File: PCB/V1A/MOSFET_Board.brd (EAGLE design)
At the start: 230 x 115 mm, 276 parts, among them IC301 7805T, IC302 7805T, J301 +12V, J302 FAN_MOLEX4PIN, J303 FAN_MOLEX4PIN, J304 DUT+, J305 DUT-, Q201 SIRC10DP, Q202 SIRC10DP, Q203 BC817, Q204 BC817, Q205 SIRC10DP, Q206 SIRC10DP, Q207 BC817, Q208 BC807, Q209 BC817, Q210 BC807, Q211 IXTK102N65X2, Q212 IXTK102N65X2, Q301 BC817, Q302 BC817, Q401 BC807, Q402 BC807, Q403 BC807, Q404 BC807, Q405 BC807, Q406 BC807, Q407 BC807, Q408 BC807, Q409 BC807, Q410 BC807, Q411 BC807, Q412 BC807, Q413 BC807, Q414 BC807, U201 AD420, U202 AD420, U203 LT1014I, U204 LT1014I, U205 AD620, U206 AD620, U207 AD620, U208 AD620, U209 LTC1865L, U210 LTC1865L, U301 LP2985-3.1, U302 LP2985-3.1, U303 AD620, U304 LTC1865L, U305 LTC1865L, U306 MAX743, U401 HCPL-063N, U402 HCPL-063N, U403 HCPL-063N, U404 HCPL-063N, U405 HCPL-063N, U406 HCPL-063N, U407 HCPL-063N

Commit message: PCB layout
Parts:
- removed HS201, HS202: (no value), mechanical:HEATSINK-LGA115X
- added C1, C2: 4µ7, passives:C3216
- added C3: 10n, passives:C2012
- added HS1: HEATSINK_LGA775, mechanical:D95263-001
- added HS2: HEATSINK_LGA115X, mechanical:E97378-001
- added U1: LP2985-3.1, ic:SOT23-5L
- JP301: device pinhead:2X03 -> mechanical:HEAD_MALE_2X3
- JP302: device pinhead:1X16 -> mechanical:HEAD_MALE_1X16
- moved R235 19.7 mm to (44.0, 2.00), turned to 270 degrees
- moved R231 19.4 mm to (44.0, 7.00), turned to 90 degrees
- moved R237 16.3 mm to (46.5, 2.00), turned to 270 degrees
- moved Q203 13.5 mm to (48.0, 7.00), turned to 180 degrees
- moved C215 13.1 mm to (49.0, 2.00), turned to 90 degrees
- moved C210 9.75 mm to (29.0, -5.75), flipped to the top, turned to 180 degrees
- moved C214 9.62 mm to (29.0, -3.50), flipped to the top, turned to 180 degrees
- moved Q207 8.50 mm to (53.0, 2.00), turned to 180 degrees
- moved D203 6.92 mm to (85.0, 2.00), turned to 180 degrees
- moved D204 6.91 mm to (61.5, 2.00), turned to 180 degrees
- moved Q208 6.40 mm to (53.0, 7.00), turned to 180 degrees
- moved C212 5.00 mm to (29.0, -8.00), flipped to the top, turned to 180 degrees
- moved C302 5.00 mm to (40.0, -4.00)
- moved C305 5.00 mm to (44.0, -1.00)
- moved C307 5.00 mm to (48.0, -4.00)
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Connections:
- new net N$66: C3.1, U1.4
- net +3V3: now also C2.1, U1.5
- net +5V: now also C1.1, U1.1, U1.3
- net GND: now also C1.2, C2.2, C3.2, U1.2
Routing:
- net +5V: track 178.9 -> 340.6 mm, vias 34 -> 36
- net CONV_C2: track 14.7 -> 134.8 mm, vias 0 -> 2
- net BYP: track 14.7 -> 131.5 mm, vias 0 -> 2
- net +12V: track 102.1 -> 202.4 mm, vias 1 -> 3
- net +3V3: track 9.05 -> 103.6 mm, vias 6 -> 7
- net CONV_V: track 53.9 -> 148.2 mm
- net CLR_DAC2: track 16.5 -> 102.5 mm, vias 1 -> 2
- net +3V_2: track 21.6 -> 80.7 mm, vias 3 -> 7
- net CONV_TEMP: track 14.7 -> 69.8 mm, vias 0 -> 2
- net GND: track 253.3 -> 308.3 mm, vias 90 -> 103
- net DUT-: track 28.3 -> 78.4 mm
- net CONV_C1: track 14.7 -> 47.9 mm, vias 0 -> 2
- net VREF2: track 10.1 -> 42.4 mm
- net -15V: track 43.0 -> 72.1 mm
- net +15V: track 89.5 -> 115.9 mm
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- removed copper zone on layer 16, net BYP2

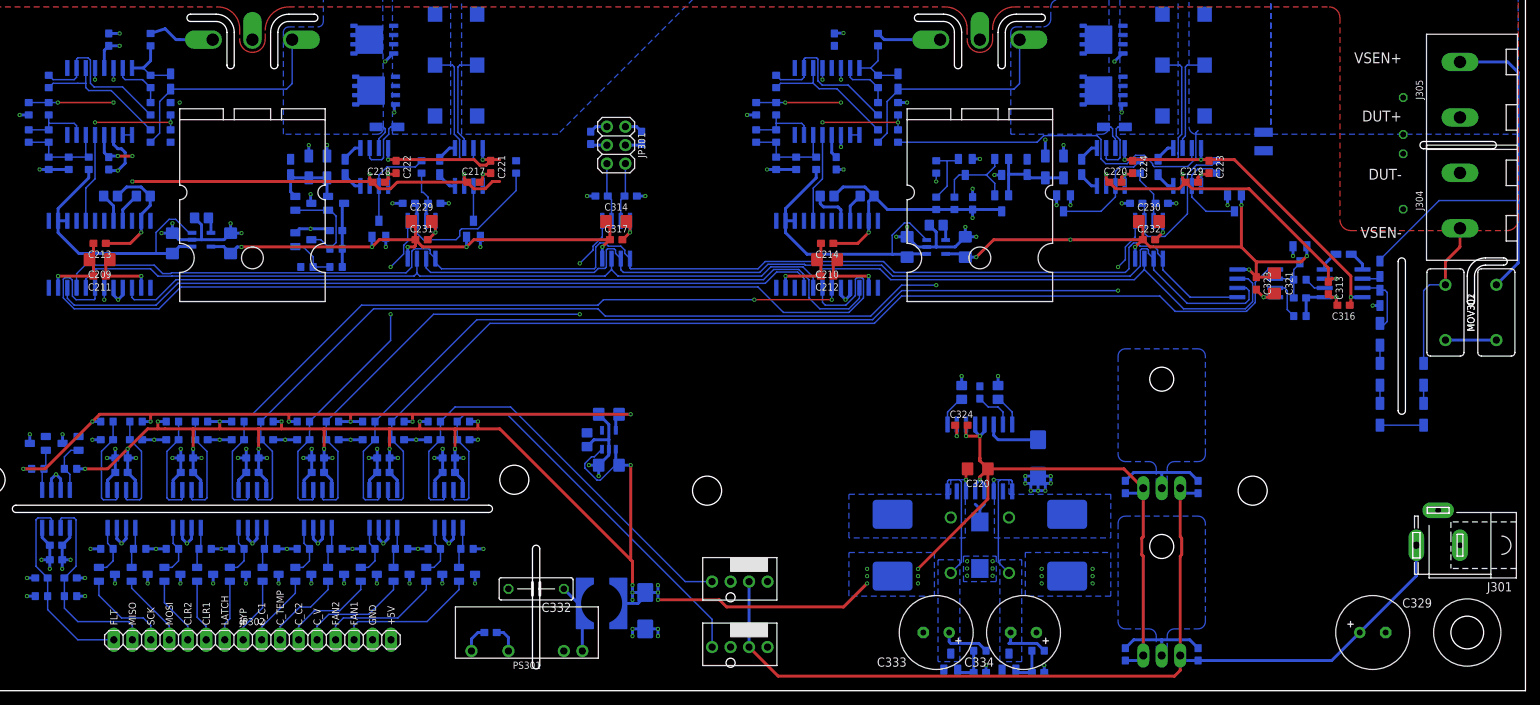
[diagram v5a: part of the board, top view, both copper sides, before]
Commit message: Finished first pass routing/layout
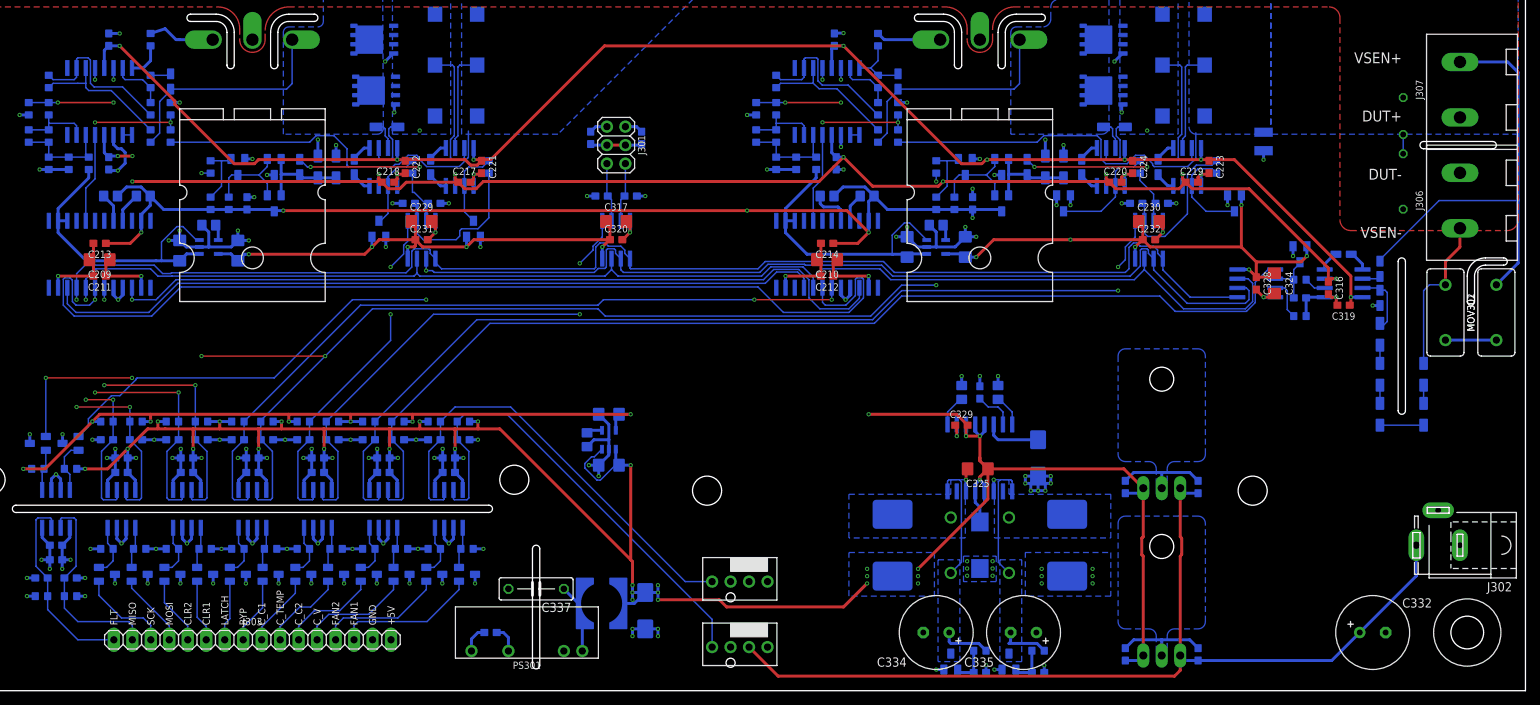
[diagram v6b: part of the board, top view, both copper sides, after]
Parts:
- removed C1, C2: 4µ7, passives:C3216
- removed C3: 10n, passives:C2012
- removed JP301: TEMP, mechanical:HEAD_MALE_2X3
- removed JP302: CTRL, mechanical:HEAD_MALE_1X16
- removed U1: LP2985-3.1, ic:SOT23-5L
- added C338, C339: 470n, passives:C1608
- added C340: 100n, passives:C1608
- added J306: DUT+, mechanical:AMPHENOL-12-762_2
- added J307: DUT-, mechanical:AMPHENOL-12-762_2
- added U307: MAX743, ic:SO16W
- C303, C317, C324: value 100n -> 4µ7; device passives:C1608 -> passives:C3216
- C304, C328: value 10n -> 100n; device passives:C2012 -> passives:C1608
- C306, C307: value 4µ7 -> 10n; device passives:C3216 -> passives:C2012
- C308, C309, C310, C325: value 470n -> 4µ7; device passives:C1608 -> passives:C3216
- C311, C313: value 100n -> 470n
- C314, C320, C321: value 4µ7 -> 100n; device passives:C3216 -> passives:C1608
- C315: value 470p -> 470n
- C318: value 100n -> 470p
- C322: value 47µ -> 100n; device passives:CT7343 -> passives:C1608
- C323: value 100n -> 47µ; device passives:C1608 -> passives:CT7343
- C329: value 220µ -> 100n; device rcl:E3,5-10 -> passives:C1608
- C330: value 10µ -> 470n; device passives:CT6032 -> passives:C1608
- C331: value 150n -> 10n; device rcl:C050-030X075 -> passives:C2012
- C332: value 470p -> 220µ; device rcl:C075-032X103 -> rcl:E3,5-10
- C333: value 220µ -> 10µ; device rcl:E3,5-10 -> passives:CT6032
- C335: value 100n -> 220µ; device passives:C1608 -> rcl:E3,5-10
- C336: value 470n -> 150n; device passives:C1608 -> rcl:C050-030X075
- C337: value 470n -> 470p; device passives:C1608 -> rcl:C075-032X103
- J301: value +12V -> TEMP; device con-jack:SPC4078 -> mechanical:HEAD_MALE_2X3
- J302: value FAN_MOLEX4PIN -> +12V; device mechanical:MOLEX_47053-1000 -> con-jack:SPC4078
- J303: value FAN_MOLEX4PIN -> CTRL; device mechanical:MOLEX_47053-1000 -> mechanical:HEAD_MALE_1X16
- J304: value DUT+ -> FAN_MOLEX4PIN; device mechanical:AMPHENOL-12-762_2 -> mechanical:MOLEX_47053-1000
- J305: value DUT- -> FAN_MOLEX4PIN; device mechanical:AMPHENOL-12-762_2 -> mechanical:MOLEX_47053-1000
- L302: value 4µ7 -> 100µ; device inductor-coilcraft:MSS7341 -> passives:MSS1260
- L303: value 100µ -> 4µ7; device passives:MSS1260 -> inductor-coilcraft:MSS7341
- U303: value AD620 -> LP2985-3.1; device ic:SO8 -> ic:SOT23-5L
- U304: value LTC1865L -> AD620
- U306: value MAX743 -> LTC1865L; device ic:SO16W -> ic:SO8
- moved J301 125.7 mm to (0.00, 10.0), turned to 270 degrees
- moved J305 119.9 mm to (17.0, -50.0), turned to 0 degrees
- moved J304 116.5 mm to (17.0, -59.0), turned to 0 degrees
- moved C332 115.2 mm to (104.0, -57.0), turned to 0 degrees
- moved U303 103.3 mm to (-1.00, -30.5), turned to 0 degrees
- moved C312 100.3 mm to (80.0, -60.0), turned to 90 degrees
- moved U304 100.2 mm to (100.0, -9.00), turned to 270 degrees
- moved C305 100.0 mm to (-56.0, -1.00)
- moved C306 97.0 mm to (44.0, -1.00), turned to 0 degrees
- moved J302 97.0 mm to (113.0, -45.0), turned to 180 degrees
- moved C336 96.1 mm to (108.2, 14.0), turned to 90 degrees
- moved C315 93.1 mm to (2.00, 3.00)
- moved U305 88.2 mm to (0.00, -3.00), turned to 180 degrees
- moved C310 81.6 mm to (-1.00, -27.0), turned to 0 degrees
- moved C335 73.3 mm to (56.0, -57.0), flipped to the top
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- renumbered HS1 to HS201, HS2 to HS202
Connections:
- net +12V: now also C312.1, C313.1, C332.+, J302.3, J304.2, J305.2; no longer C309.1, C310.1, C329.+, J301.3, J302.2, J303.2
- net +15V: now also C316.1, Q302.2, U304.7; no longer C313.1, Q301.2, U303.7
- net +3V3: now also C310.1, U303.5; no longer C2.1, U1.5
- net +3V_1: now also C308.1, C320.1, U305.8; no longer C306.1, C314.1, U304.8
- net +3V_2: now also C309.1, C324.1, C328.1, U306.8; no longer C307.1, C321.1, C323.1, U305.8
- net +5V: now also C304.1, C314.1, C321.1, C322.1, C323.+, C325.1, C329.2, C333.+, J301.3, J301.4, L301.1, L303.2, U303.1, U303.3, U307.12, U307.13, U307.3, U307.4, U307.5; no longer C1.1, C311.1, C318.1, C319.1, C320.1, C322.+, C324.2, C330.+, JP301.3, JP301.4, L302.2, L303.1, U1.1, U1.3, U306.12, U306.13, U306.3, U306.4, U306.5
- net +5V_I: now also C337.2, C340.1, J303.16; no longer C332.2, C335.1, JP302.16
- net -15V: now also C319.1, Q301.2, U304.4; no longer C316.1, Q302.2, U303.4
- net BYP_I: now also J303.8; no longer JP302.8
- net CLR_DAC1_I: now also J303.6; no longer JP302.6
- net CLR_DAC2: now also C413.1, R413.1, U401.6; no longer C427.1, R427.1, U406.6
- net CLR_DAC2_I: now also J303.7, Q405.1; no longer JP302.5, Q413.1
- net CONV_C1_I: now also J303.9; no longer JP302.9
- net CONV_C2_I: now also J303.11; no longer JP302.11
- net CONV_TEMP: now also U305.1; no longer U304.1
- net CONV_TEMP_I: now also J303.10; no longer JP302.10
- net CONV_V: now also U306.1; no longer U305.1
- net CONV_V_I: now also J303.12; no longer JP302.12
- net DUT+: now also J306.2; no longer J304.2
- net DUT-: now also C336.2, J307.1; no longer C331.2, J305.1
- net FAN1_PWM: now also J304.4; no longer J302.4
- net FAN1_PWM_I: now also J303.14; no longer JP302.14
- net FAN1_SIG: now also J304.3; no longer J302.3
- net FAN2_PWM: now also J305.4; no longer J303.4
- net FAN2_PWM_I: now also J303.13; no longer JP302.13
- net FAN2_SIG: now also J305.3; no longer J303.3
- net FLT_DAC_I: now also J303.1; no longer JP302.1
- net GND: now also C322.2, C323.-, C324.2, C329.1, C330.2, C331.2, C332.-, C334.-, C335.+, C338.2, C339.2, J301.2, J304.1, J305.1, L302.2, U303.2, U304.5, U306.4, U307.11, U307.14, U307.2; no longer C1.2, C2.2, C3.2, C322.-, C323.2, C324.1, C329.-, C330.-, C334.+, C336.2, C337.2, J303.1, JP301.1, JP301.2, L301.2, U1.2, U303.5, U304.4, U306.11, U306.14, U306.2
- net GNDI: now also C340.2, J303.15; no longer C335.2, JP302.15
- net LATCH_DAC: now also C427.1, R427.1, U406.6; no longer C413.1, R413.1, U401.6
- net LATCH_DAC_I: now also J303.5, Q413.1; no longer JP302.7, Q405.1
- net MISO: now also U306.6; no longer U304.6
- net MISO_I: now also J303.2; no longer JP302.2
- net MOSI: now also U306.5; no longer U304.5
- net MOSI_I: now also J303.4; no longer JP302.4
- net N$10: now also C305.1; no longer C304.1
- net N$23: now also U304.6; no longer U303.6
- net N$29: now also U304.3; no longer U303.3
- net N$30: now also C318.1, U306.2; no longer C315.1, U305.2
- net N$32: now also C334.+, Q302.3, U307.16; no longer C333.+, Q301.3, U306.16
- net N$34: now also C331.1, U307.8; no longer C328.1, U306.8
- net N$35: now also C330.1, U307.7; no longer C325.1, U306.7
- net N$36: now also U304.2; no longer U303.2
- net N$37: now also U307.1; no longer U306.1
- net N$38: now also L301.2, U307.15; no longer L303.2, U306.15
- net N$39: now also L302.1, U307.10; no longer L301.1, U306.10
- net N$45: now also U306.3; no longer U305.3
- net N$60: now also C337.1, L303.1; no longer C332.1, L302.1
- net N$61: now also C336.1; no longer C331.1
- net N$62: now also C306.1; no longer C305.1
- net N$63: now also C339.1, Q302.1; no longer C336.1, Q301.1
- net N$64: now also C335.-, Q301.3, U307.9; no longer C334.-, Q302.3, U306.9
- net N$65: now also C338.1, Q301.1; no longer C337.1, Q302.1
- net N$66: now also C307.1, U303.4; no longer C3.1, U1.4
- net RG1_H6: now also U304.1; no longer U303.1
- net RG2_H6: now also U304.8; no longer U303.8
- net SCK: now also U306.7; no longer U304.7
- net SCK_I: now also J303.3; no longer JP302.3
- net TEMP1: now also C311.1, J301.5, U305.2; no longer C308.1, JP301.5, U304.2
- net TEMP2: now also C315.1, J301.6, U305.3; no longer C312.1, JP301.6, U304.3
- net VREF_MAX743: now also U307.6; no longer U306.6
- net VSENSE+: now also J306.1; no longer J304.1
- net VSENSE-: now also J307.2; no longer J305.2
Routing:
- net -15V: track 72.1 -> 292.1 mm, vias 6 -> 9
- net +15V: track 115.9 -> 274.3 mm, vias 8 -> 11
- net +12V: track 202.4 -> 345.5 mm, vias 3 -> 5
- net +5V: track 340.6 -> 447.8 mm, vias 36 -> 37
- net MISO: track 131.3 -> 191.8 mm, vias 0 -> 2
- net DUT-: track 78.4 -> 127.8 mm
- net BYP: track 131.5 -> 175.0 mm, vias 2 -> 5
- net LATCH_DAC: track 153.3 -> 184.0 mm, vias 0 -> 3
- net FLT_DAC: track 109.5 -> 139.8 mm, vias 0 -> 3
- net CLR_DAC1: track 16.3 -> 45.6 mm, vias 1 -> 3
- net MOSI: track 196.0 -> 221.6 mm, vias 0 -> 3
- net SCK: track 195.1 -> 217.3 mm, vias 0 -> 3
- net CSEN_H2: track 28.3 -> 50.0 mm, vias 0 -> 3
- net CSEN_H1: track 28.8 -> 49.9 mm, vias 0 -> 3
- net N$7: track 4.80 -> 11.3 mm
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
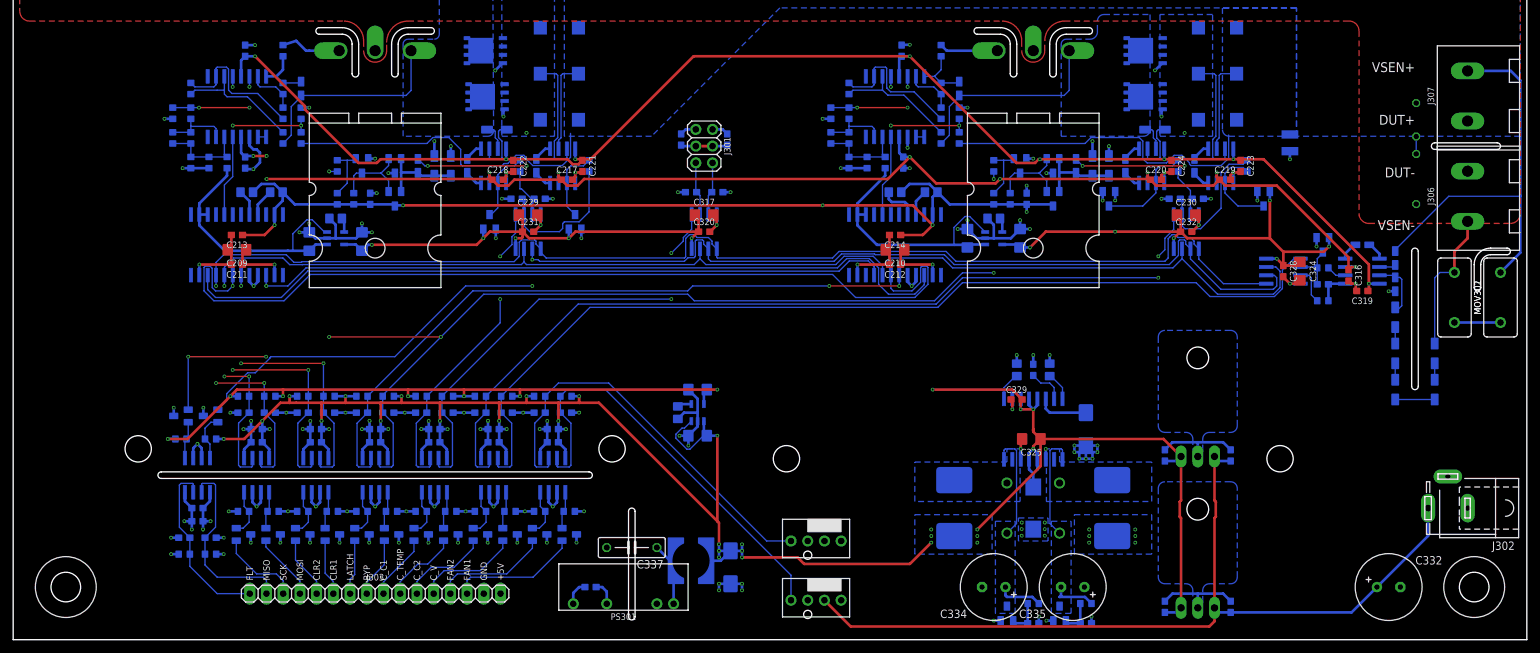
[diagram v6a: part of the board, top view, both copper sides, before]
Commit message: PCB layout
Added some copper pours.
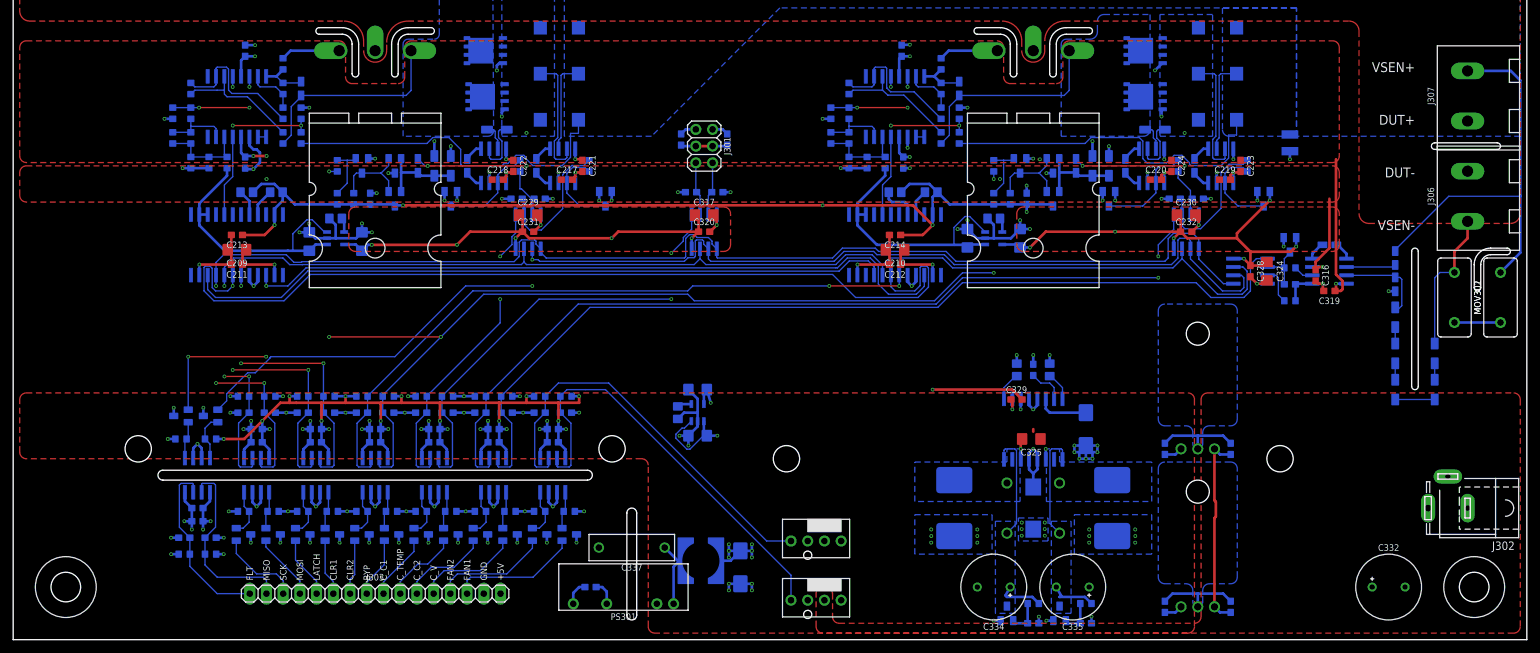
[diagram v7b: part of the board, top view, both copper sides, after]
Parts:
- removed C336: 150n, rcl:C050-030X075
- removed R311: 16R, rcl:0204/7
- C201, C202, C203, C204, C211, C212, C213, C214, C215, C216, C217, C218, C219, C220, C221, C222, C223, C224, C225, C226, C227, C228, C231, C232, C304, C311, C312, C313, C314, C315, C316, C318, C319, C320, C321, C322, C328, C329, C330, C338, C339, C340, C401, C402, C403, C404, C405, C406, C407, C408, C409, C410, C411, C412, C413, C414, C415, C416, C417, C418, C419, C420, C421, C422, C423, C424, C425, C426, C427, C428: device passives:C1608 -> passives:CAPC1608
- C205, C206, C207, C208, C305, C306, C307, C326, C331: device passives:C2012 -> passives:CAPC2012
- C209, C210, C229, C230, C301, C302, C303, C308, C309, C310, C317, C324, C325: device passives:C3216 -> passives:CAPC3216
- C323: device passives:CT7343 -> passives:CAPCP7343
- C327, C333: device passives:CT6032 -> passives:CAPCP6032
- C332, C334, C335: device rcl:E3,5-10 -> passives:CAPPRD500W60D1000H
- C337: device rcl:C075-032X103 -> passives:CAPRR1000W80L1300T400H900
- IC301, IC302: value 7805T -> 78L05_TO-220AB-3-BR; device linear:TO220H -> ic:TO-220AB-3-BR
- R201, R202, R203, R204, R205, R206, R207, R208, R209, R210, R211, R212, R213, R214, R215, R216, R217, R218, R219, R220, R221, R222, R223, R224, R225, R226, R229, R230, R231, R233, R235, R236, R237, R239, R255, R256, R257, R258, R309, R310, R312, R313, R401, R402, R403, R404, R405, R406, R407, R408, R409, R410, R411, R412, R413, R414, R415, R416, R417, R418, R419, R420, R421, R422, R423, R424, R425, R426, R427, R428: device passives:R1608 -> passives:RESC1608
- R227, R228, R247, R248, R251, R252, R253, R254, R302, R307, R308: device passives:R2012W -> passives:RESC2012
- R232, R234, R238, R240, R243, R245, R301, R303, R304, R305, R306: device passives:R3216W -> passives:RESC3216
- R241, R242, R244, R246, R249, R250: device passives:R6332W -> passives:RESC6332
- moved IC301 10.0 mm to (75.0, -60.0)
- moved IC302 9.00 mm to (75.0, -36.0)
- moved D202 6.85 mm to (-38.5, 2.00), turned to 180 degrees
- moved D201 5.79 mm to (-15.0, 2.00), turned to 180 degrees
- moved C316 5.00 mm to (92.9, -9.63)
- moved C318 5.00 mm to (89.0, -11.0)
- moved C319 5.00 mm to (95.0, -12.0)
- moved C324 5.00 mm to (85.5, -9.00)
- moved C328 5.00 mm to (83.0, -9.00)
- moved D301 5.00 mm to (89.0, -5.00)
- moved R308 5.00 mm to (95.0, -5.00)
- moved R309 5.00 mm to (89.0, -8.50)
- moved R310 5.00 mm to (89.0, -13.5)
- moved U304 5.00 mm to (95.0, -9.00)
- moved U306 5.00 mm to (83.0, -9.00)
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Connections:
- removed net N$61: C336.1, R311.1
- net DUT+: no longer R311.2
- net DUT-: no longer C336.2
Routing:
- net -15V: track 292.1 -> 115.7 mm
- net +15V: track 274.3 -> 104.2 mm
- net +5V: track 447.8 -> 298.7 mm
- net +12V: track 345.5 -> 244.3 mm
- net +3V3: track 103.6 -> 13.5 mm
- net +3V_1: track 71.2 -> 83.1 mm, vias 5 -> 7
- net DUT-: track 127.8 -> 134.6 mm
- net N$36: track 2.53 -> 7.53 mm
- net N$29: track 9.27 -> 14.3 mm
- net SCK: track 217.3 -> 212.6 mm
- net CONV_V: track 148.2 -> 144.0 mm
- net MOSI: track 221.6 -> 217.7 mm
- net N$16: track 11.2 -> 15.0 mm
- net MISO: track 191.8 -> 188.5 mm
- net +3V_2: track 80.7 -> 77.7 mm
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- added copper zone on layer 1, net +12V
- added copper zone on layer 1, net +15V
- added copper zone on layer 2, net +3V3
- added copper zone on layer 1, net +3V_1
- added copper zone on layer 1, net +3V_2
- added copper zone on layer 1, net +5V
- added copper zone on layer 1, net -15V
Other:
- outline, holes or cut-outs redrawn

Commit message: PCB layout
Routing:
- net -15V: track 115.7 -> 114.4 mm
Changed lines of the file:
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@@
 <layer number="13" name="Route13" color="21" fill="1" visible="no" active="no"/>
 <layer number="14" name="Route14" color="22" fill="1" visible="no" active="no"/>
-<layer number="15" name="Route15" color="23" fill="1" visible="no" active="yes"/>
+<layer number="15" name="Route15" color="23" fill="1" visible="yes" active="yes"/>
 <layer number="16" name="Bottom" color="1" fill="1" visible="yes" active="yes"/>
 <layer number="17" name="Pads" color="2" fill="1" visible="yes" active="yes"/>
@@
 <via x="-19.595" y="8" extent="1-16" drill="0.3" diameter="0.6"/>
 <wire x1="80.405" y1="9.6" x2="80.405" y2="8" width="0.4064" layer="16"/>
-<wire x1="81.5" y1="7.85" x2="81.35" y2="8" width="0.4064" layer="1"/>
 <via x="69.905" y="8" extent="1-16" drill="0.3" diameter="0.6"/>
-<wire x1="70" y1="8" x2="69.905" y2="8" width="0.4064" layer="1"/>
-<wire x1="70.85" y1="8" x2="71" y2="7.85" width="0.4064" layer="1"/>
 <wire x1="69.905" y1="9.6" x2="69.905" y2="8" width="0.4064" layer="16"/>
-<wire x1="71" y1="7.85" x2="71.15" y2="8" width="0.4064" layer="1"/>
 <contactref element="Q301" pad="2"/>
 <via x="96" y="-10.905" extent="1-16" drill="0.3" diameter="0.6"/>
@@
 <wire x1="-18.65" y1="8" x2="-19.595" y2="8" width="0.4064" layer="1"/>
 <wire x1="-28.85" y1="8" x2="-29" y2="7.85" width="0.4064" layer="1"/>
-<wire x1="-18.5" y1="7.85" x2="-18.35" y2="8" width="0.4064" layer="1"/>
-<wire x1="81.65" y1="8" x2="81.5" y2="7.85" width="0.4064" layer="1"/>
 <via x="31.25" y="23.65" extent="1-16" drill="0.3" diameter="0.6"/>
 <wire x1="30" y1="23.65" x2="31.25" y2="23.65" width="0.4064" layer="16"/>
 <wire x1="29.635" y1="20.6" x2="29.635" y2="23.285" width="0.4064" layer="16"/>
 <wire x1="29.635" y1="23.285" x2="30" y2="23.65" width="0.4064" layer="16"/>
-<wire x1="50.8271625" y1="8" x2="51" y2="8" width="0.4064" layer="1"/>
 <via x="52" y="-62.1" extent="1-16" drill="0.3" diameter="0.6"/>
 <wire x1="53.05" y1="-62.1" x2="52" y2="-62.1" width="0.4064" layer="16"/>
